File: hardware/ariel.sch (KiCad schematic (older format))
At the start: 19 parts, among them SW1 SW_Push, U1 WeMos_Battery_Shield, U2 Si7020-A20, U3 WeMos_D1_mini, U4 74HC595

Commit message: Update symbols for wemos and shield
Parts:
- removed U3: WeMos_D1_mini, symbol wemos_mini:WeMos_D1_mini
- added U2: WeMos_D1_mini, symbol wemos_mini:WeMos_D1_mini
- renumbered R4 to R1, R5 to R2, R6 to R3, R7 to R4, R8 to R5, R3 to R6, R1 to R7, R2 to R8, U4 to U3, U2 to U4
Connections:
- wire segments 65 -> 60
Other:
- note added: "WeMos Battery shield is \nconnected to a LiPo battery."
- note removed: "WeMos Battery shield is connected to a LiPo battery."
- moved on the sheet: C1, D1, D2, D3, D4, D5, R1, R2, R3, R4, R5, R6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

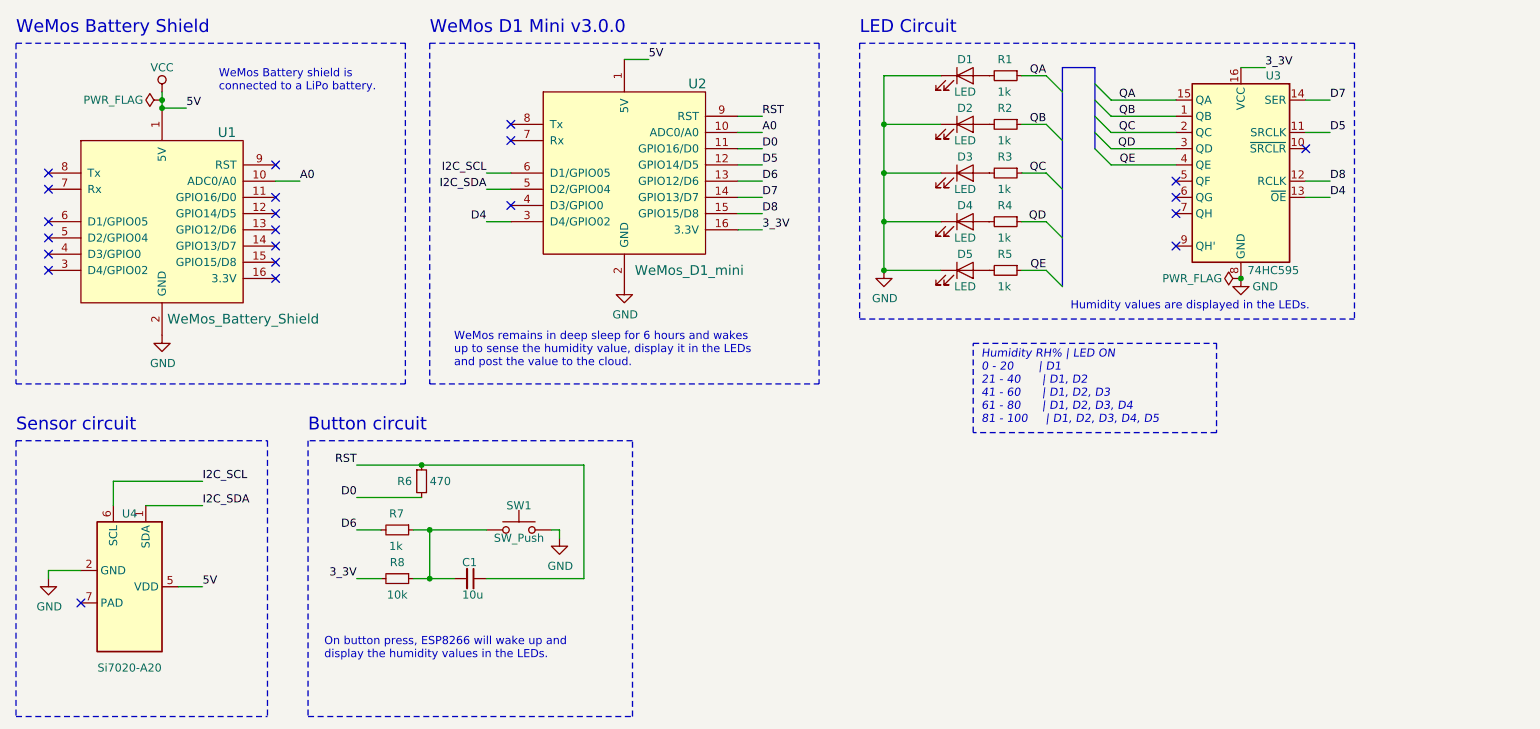
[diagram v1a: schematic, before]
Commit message: Add new symbol for Si7021 breakout board
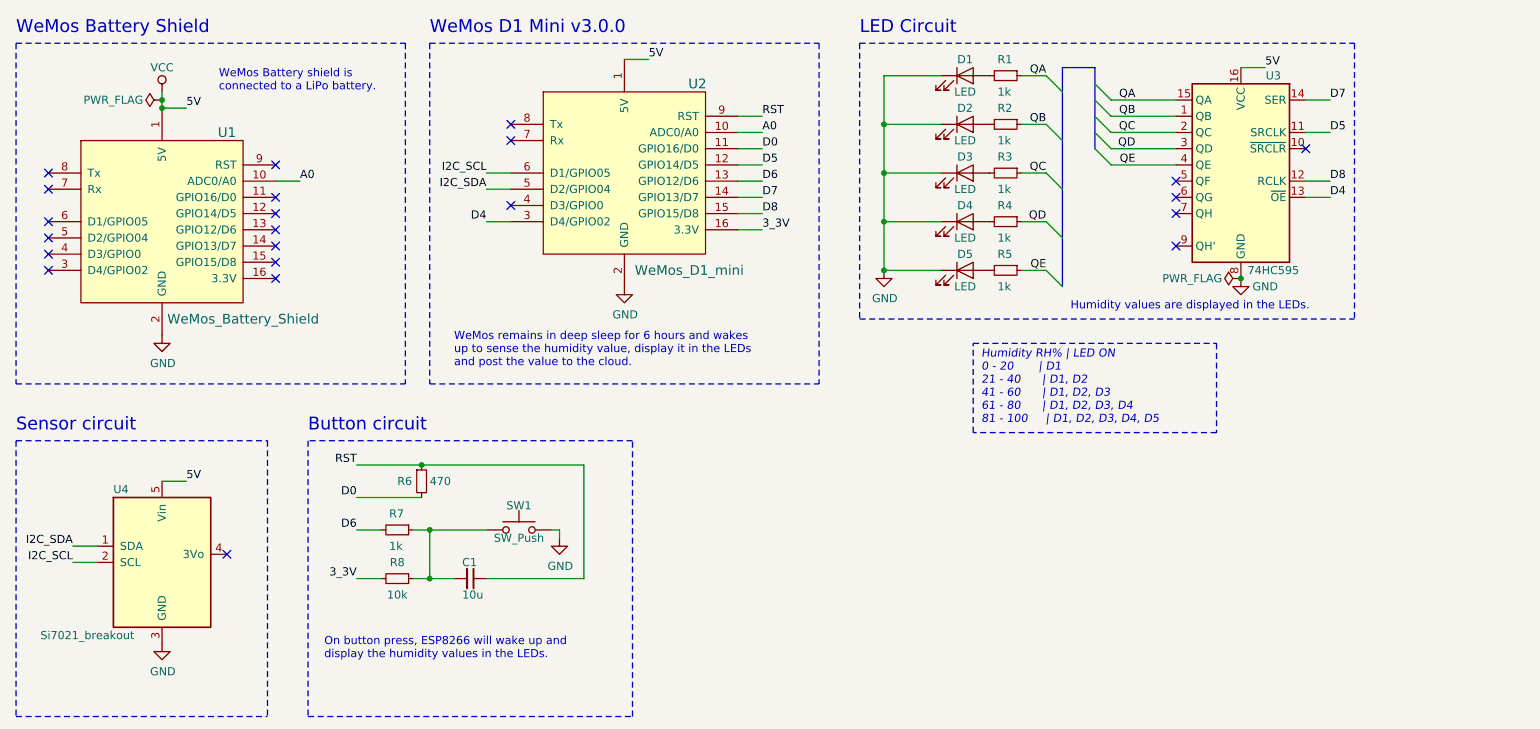
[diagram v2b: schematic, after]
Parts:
- removed U4: Si7020-A20, Package_DFN_QFN:DFN-6-1EP_3x3mm_P1mm_EP1.5x2.4mm, symbol Sensor_Humidity:Si7020-A20
- added U4: Si7021_breakout, symbol Si7021_breakout_board:Si7021_breakout
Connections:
- net 3_3V: no longer U3.16 (VCC)
- net GND: now also U4.3 (GND)
- net I2C_SCL: now also U4.2 (SCL)
- net I2C_SDA: now also U4.1 (SDA)
- net VCC: now also U3.16 (VCC), U4.5 (Vin)
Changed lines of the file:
@@
 $EndComp
-$Comp
-L Sensor_Humidity:Si7020-A20 U4
-U 1 1 5C86A90D
-P 1600 4250
-F 0 "U4" V 1150 4250 50  0000 C CNN
-F 1 "Si7020-A20" V 2100 4250 50  0000 C CNN
-F 2 "Package_DFN_QFN:DFN-6-1EP_3x3mm_P1mm_EP1.5x2.4mm" H 1600 3850 50  0001 C CNN
-F 3 "https://www.silabs.com/documents/public/data-sheets/Si7020-A20.pdf" H 1400 4550 50  0001 C CNN
-	1    1600 4250
-	0    1    1    0
-$EndComp
-NoConn ~ 1300 4350
 $Comp
 L Device:R_Small R1
@@
 Text Notes 900  850  0    79   ~ 0
 WeMos Battery Shield
-Text Label 2050 3600 0    50   ~ 0
+Text Label 1250 4100 2    50   ~ 0
 I2C_SCL
-Text Label 2050 3750 0    50   ~ 0
+Text Label 1250 4000 2    50   ~ 0
 I2C_SDA
 $Comp
 L power:GND #PWR01
 U 1 1 5C89C91B
-P 1100 4200
-F 0 "#PWR01" H 1100 3950 50  0001 C CNN
-F 1 "GND" H 1105 4027 50  0000 C CNN
-F 2 "" H 1100 4200 50  0001 C CNN
-F 3 "" H 1100 4200 50  0001 C CNN
-	1    1100 4200
-	1    0    0    -1
-$EndComp
-Wire Wire Line
-	1300 4150 1100 4150
-Wire Wire Line
-	1100 4150 1100 4200
+P 1800 4600
+F 0 "#PWR01" H 1800 4350 50  0001 C CNN
+F 1 "GND" H 1805 4427 50  0000 C CNN
+F 2 "" H 1800 4600 50  0001 C CNN
+F 3 "" H 1800 4600 50  0001 C CNN
+	1    1800 4600
+	1    0    0    -1
+$EndComp
 Text Label 5500 2050 0    50   ~ 0
 3_3V
-Text Label 2050 4250 0    50   ~ 0
+Text Label 8600 1050 0    50   ~ 0
 5V
-Text Label 8600 1050 0    50   ~ 0
-3_3V
 Text Label 5500 1950 0    50   ~ 0
 D8
@@
 Text Notes 6100 850  0    79   ~ 0
 LED Circuit
-Wire Wire Line
-	1900 4250 2050 4250
-Wire Wire Line
-	1500 3750 1500 3600
-Wire Wire Line
-	1700 3750 2050 3750
-Wire Wire Line
-	1500 3600 2050 3600
 Wire Notes Line
 	900  3350 900  5050
@@
 Wire Notes Line
 	5850 900  5850 3000
+$Comp
+L Si7021_breakout_board:Si7021_breakout U4
+U 1 1 5C97D9C5
+P 1800 4100
+F 0 "U4" H 1500 4550 50  0000 L CNN
+F 1 "Si7021_breakout" H 1050 3650 50  0000 L CNN
+F 2 "" H 1800 3500 50  0000 C CNN
+F 3 "http://ams.com/eng/Products/Environmental-Sensors/Air-Quality-Sensors/CCS811" H 1800 3900 50  0001 C CNN
+	1    1800 4100
+	1    0    0    -1
+$EndComp
+Wire Wire Line
+	1400 4000 1250 4000
+Wire Wire Line
+	1400 4100 1250 4100
+Text Label 1950 3600 0    50   ~ 0
+5V
+Wire Wire Line
+	1800 3600 1950 3600
+NoConn ~ 2200 4050
 Wire Bus Line
 	7550 1050 7550 1550

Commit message: Display humidity values with shift register and LEDs
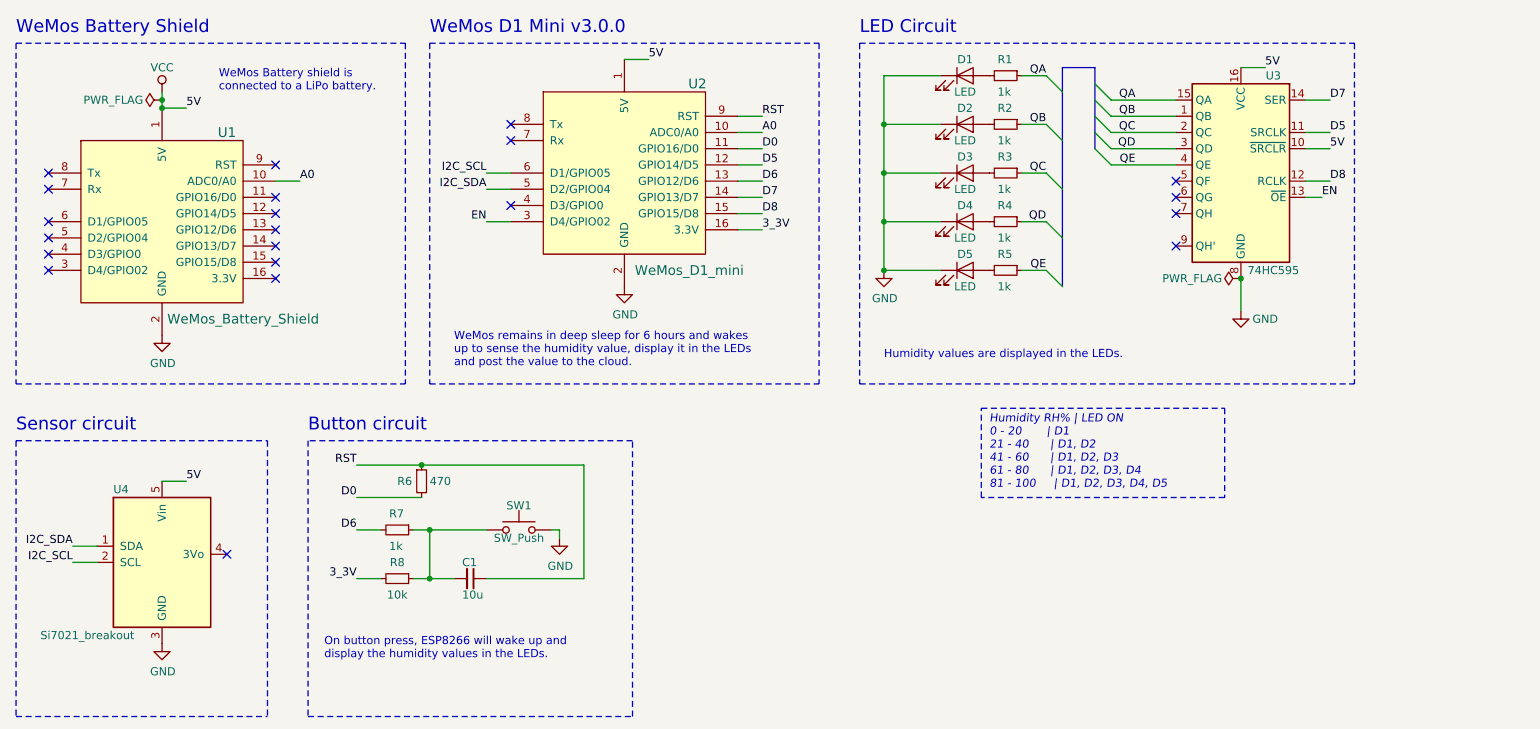
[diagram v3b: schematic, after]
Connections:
- net VCC: now also U3.10 (~SRCLR)
- net D4 renamed EN
- no-connect marks 22 -> 21
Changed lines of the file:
@@
 L power:GND #PWR07
 U 1 1 5C8625CA
-P 8450 2350
-F 0 "#PWR07" H 8450 2100 50  0001 C CNN
-F 1 "GND" H 8600 2300 50  0000 C CNN
-F 2 "" H 8450 2350 50  0001 C CNN
-F 3 "" H 8450 2350 50  0001 C CNN
-	1    8450 2350
+P 8450 2550
+F 0 "#PWR07" H 8450 2300 50  0001 C CNN
+F 1 "GND" H 8600 2500 50  0000 C CNN
+F 2 "" H 8450 2550 50  0001 C CNN
+F 3 "" H 8450 2550 50  0001 C CNN
+	1    8450 2550
 	1    0    0    -1
 $EndComp
@@
 	1    0    0    -1
 $EndComp
-NoConn ~ 8850 1550
 NoConn ~ 8050 1750
 NoConn ~ 8050 1850
@@
 Text Label 3800 1800 2    50   ~ 0
 I2C_SDA
-Text Label 3800 2000 2    50   ~ 0
-D4
 Text Label 5500 1350 0    50   ~ 0
 RST
@@
 Text Label 9000 1750 0    50   ~ 0
 D8
-Text Label 9000 1850 0    50   ~ 0
-D4
 Text Label 9000 1250 0    50   ~ 0
 D7
@@
 	8850 1750 9000 1750
 Wire Wire Line
-	8850 1850 9000 1850
-Wire Wire Line
 	8450 1050 8600 1050
 $Comp
@@
 Text Label 7250 2300 2    50   ~ 0
 QE
-Wire Notes Line
-	6100 900  6100 2600
 Text Notes 6100 850  0    79   ~ 0
 LED Circuit
@@
 Text Notes 3600 2900 0    50   ~ 0
 WeMos remains in deep sleep for 6 hours and wakes \nup to sense the humidity value, display it in the LEDs \nand post the value to the cloud.
-Text Notes 6850 3250 0    50   Italic 0
+Text Notes 6900 3650 0    50   Italic 0
 Humidity RH% | LED ON\n0 - 20       | D1\n21 - 40      | D1, D2\n41 - 60      | D1, D2, D3\n61 - 80      | D1, D2, D3, D4\n81 - 100     | D1, D2, D3, D4, D5
 Wire Notes Line
-	6800 2750 8300 2750
-Wire Notes Line
-	8300 3300 6800 3300
-Wire Notes Line
-	6800 3300 6800 2750
-Wire Notes Line
-	8300 2750 8300 3300
-Text Notes 7400 2550 0    50   ~ 0
+	6850 3150 8350 3150
+Wire Notes Line
+	8350 3700 6850 3700
+Wire Notes Line
+	6850 3700 6850 3150
+Wire Notes Line
+	8350 3150 8350 3700
+Text Notes 6250 2850 0    50   ~ 0
 Humidity values are displayed in the LEDs.
-Wire Notes Line
-	9150 900  9150 2600
-Wire Notes Line
-	6100 2600 9150 2600
 Wire Notes Line
 	6100 900  9150 900
@@
 Wire Notes Line
 	900  5050 2450 5050
-Connection ~ 8450 2350
 NoConn ~ 1100 2300
 Wire Notes Line
@@
 	900  900  900  3000
 Wire Wire Line
-	3950 2000 3800 2000
-Wire Wire Line
 	4650 1000 4800 1000
 Wire Notes Line
@@
 F 1 "Si7021_breakout" H 1050 3650 50  0000 L CNN
 F 2 "" H 1800 3500 50  0000 C CNN
-F 3 "http://ams.com/eng/Products/Environmental-Sensors/Air-Quality-Sensors/CCS811" H 1800 3900 50  0001 C CNN
+F 3 "https://learn.adafruit.com/adafruit-si7021-temperature-plus-humidity-sensor/downloads" H 1800 3900 50  0001 C CNN
 	1    1800 4100
 	1    0    0    -1
@@
 	1800 3600 1950 3600
 NoConn ~ 2200 4050
+Wire Wire Line
+	8850 1850 8950 1850
+Connection ~ 8450 2350
+Wire Notes Line
+	6100 3000 9150 3000
+Wire Notes Line
+	6100 900  6100 3000
+Wire Notes Line
+	9150 900  9150 3000
+Wire Wire Line
+	8850 1550 9000 1550
+Text Label 9000 1550 0    50   ~ 0
+5V
+Wire Wire Line
+	3950 2000 3800 2000
+Text Label 3800 2000 2    50   ~ 0
+EN
+Wire Wire Line
+	8450 2350 8450 2550
 Wire Bus Line
 	7550 1050 7550 1550
 Wire Bus Line
 	7350 1050 7350 2400
+Text Label 8950 1850 0    50   ~ 0
+EN
 $EndSCHEMATC
